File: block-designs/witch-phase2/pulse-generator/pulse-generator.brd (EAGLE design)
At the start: 159.8 x 99.1 mm, 63 parts, among them IC1 74LVC1G08DBV, IC10 74LVC1G08DBV, IC11 741G175, IC12 74LVC1G08DBV, IC13 741G175, IC14 741G175, IC15 741G175, IC16 74LVC1G04DBV, IC17 741G175, IC18 74LVC1G04DBV, IC19 74LVC1G04DBV, IC2 741G175, IC20 NE555D, IC21 74LVC1G17DBV, IC22 74LVC1G17DBV, IC23 74LVC1G17DBV, IC3 741G175, IC4 741G175, IC5 74LVC1G04DBV, IC6 74LVC1G08DBV, IC7 741G175, IC8 74LVC1G08DBV, IC9 74LVC1G08DBV, J1 POWER_JACKPTH, Q1 MMBT2907ALT1SMD

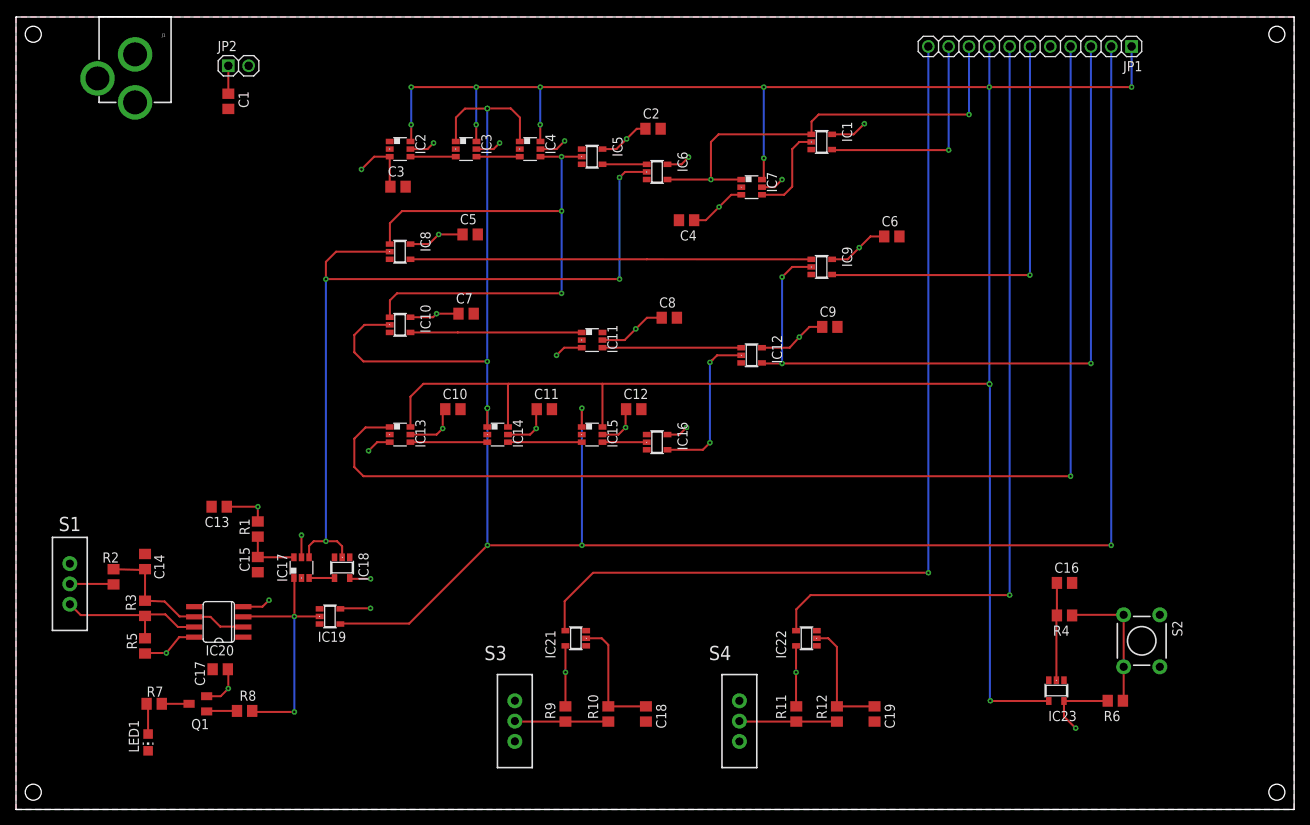
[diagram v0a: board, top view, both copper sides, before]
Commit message: switch position tweaks and drc fixes
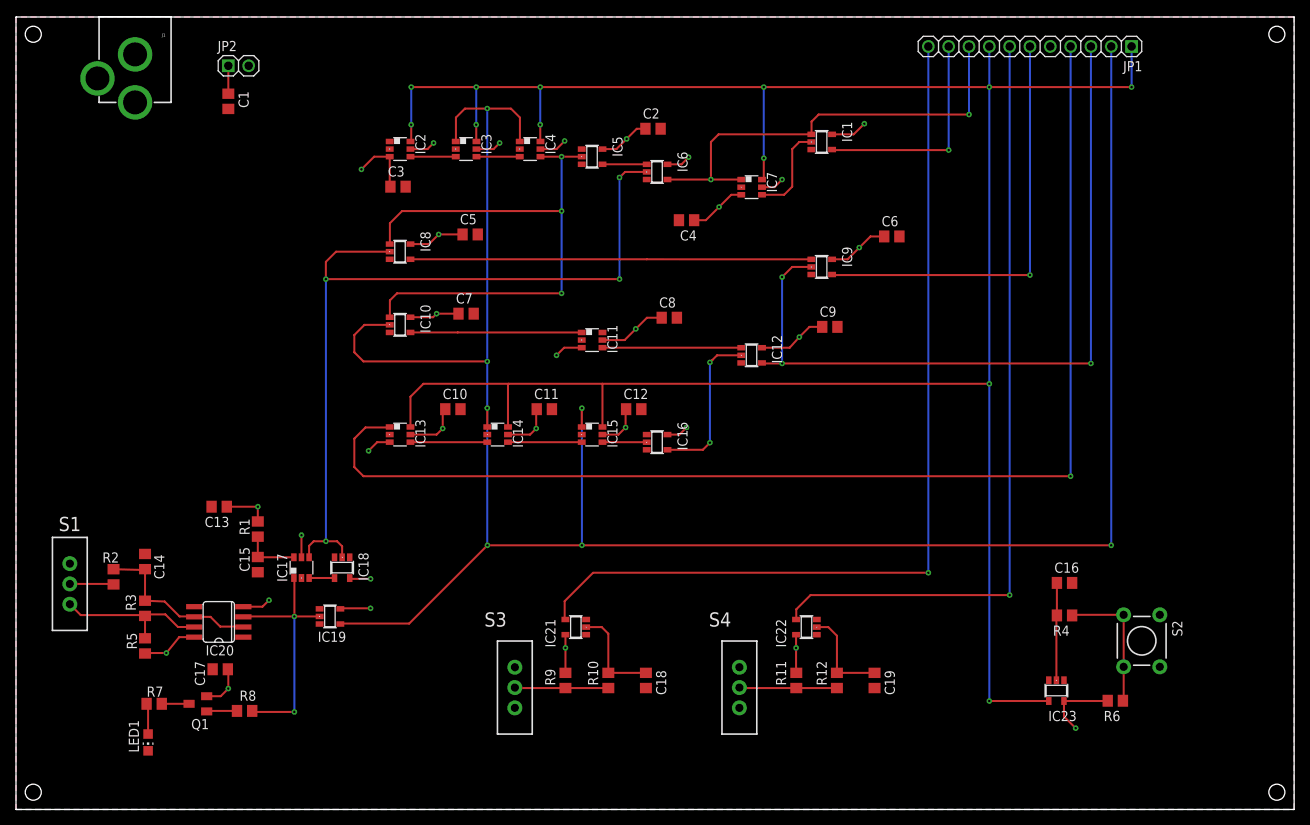
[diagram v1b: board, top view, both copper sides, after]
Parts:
- moved C18 4.19 mm to (78.7, 16.1)
- moved C19 4.19 mm to (107.3, 16.1)
- moved R10 4.19 mm to (74.0, 16.1)
- moved R11 4.19 mm to (97.5, 16.1)
- moved R12 4.19 mm to (102.6, 16.1)
- moved R9 4.19 mm to (68.7, 16.1)
- moved S3 4.19 mm to (62.4, 15.2)
- moved S4 4.19 mm to (90.4, 15.2)
- moved IC21 1.40 mm to (70.0, 22.8)
- moved IC22 1.40 mm to (98.8, 22.8)
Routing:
- net VCC: track 167.7 -> 162.1 mm
- net N$29: track 15.1 -> 12.3 mm
- net N$21: track 15.5 -> 12.7 mm
- net ADD/COMP: track 98.7 -> 97.3 mm
- net CLR: track 116.5 -> 115.1 mm
- net !RST: vias 13 -> 12
- net !MCLK: vias 9 -> 7

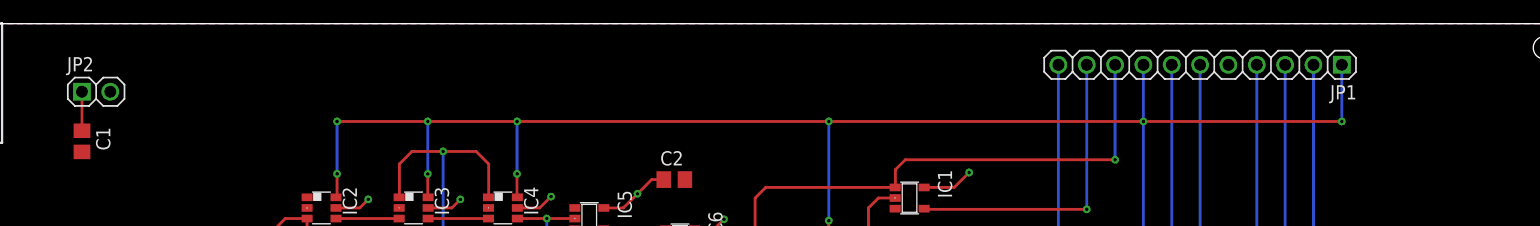
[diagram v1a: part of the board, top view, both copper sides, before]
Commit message: add labels and move downstream power connector
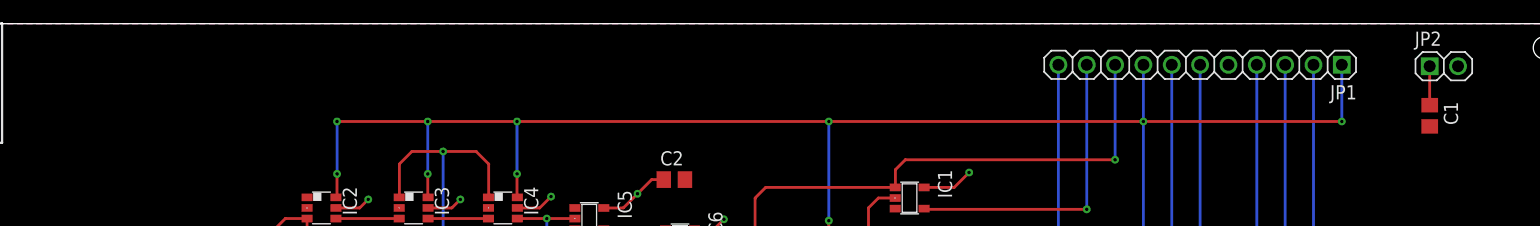
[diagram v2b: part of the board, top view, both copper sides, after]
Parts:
- moved JP2 120.8 mm to (148.6, 95.2)
- moved C1 120.8 mm to (147.3, 90.8)
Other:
- board text added: "ADD/COMP"
- board text added: "CLEAR"
- board text added: "MCLK"
- board text added: "RESET"
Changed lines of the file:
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@@
 <circle x="2.159" y="2.159" radius="2.0066" width="0.0254" layer="42"/>
 <wire x1="159.766" y1="0" x2="0" y2="0" width="0" layer="20"/>
-<text x="36.449" y="91.694" size="2.1844" layer="48">Pulse Generator
+<text x="3.048" y="73.787" size="2.1844" layer="48">Pulse Generator
 http://www.witch-e.org</text>
+<text x="56.388" y="6.096" size="1.778" layer="48">ADD/COMP</text>
+<text x="86.741" y="5.969" size="1.778" layer="48">CLEAR</text>
+<text x="142.113" y="12.446" size="1.778" layer="48">RESET</text>
+<text x="18.923" y="7.239" size="1.778" layer="48">MCLK</text>
 </plain>
 <attributes>
@@
 <element name="IC14" library="witch-e" package="DBV_R-PDSO-G6" value="741G175" x="60.198" y="46.863" rot="R270"/>
 <element name="IC15" library="witch-e" package="DBV_R-PDSO-G6" value="741G175" x="72.009" y="46.863" rot="R270"/>
-<element name="C1" library="resistor" package="C0805" value="10uF" x="26.543" y="88.519" rot="R270"/>
+<element name="C1" library="resistor" package="C0805" value="10uF" x="147.32" y="90.805" rot="R270"/>
 <element name="C17" library="resistor" package="C0805" value="10uF" x="25.527" y="17.526" smashed="yes" rot="R180">
 <attribute name="NAME" x="22.352" y="18.542" size="1.27" layer="25" rot="R270"/>
@@
 <element name="C9" library="resistor" package="C0805" value="1uF" x="101.727" y="60.325"/>
 <element name="C3" library="resistor" package="C0805" value="1uF" x="47.752" y="77.851"/>
-<element name="JP2" library="pinhead" package="1X02" value="" x="27.813" y="92.964"/>
+<element name="JP2" library="pinhead" package="1X02" value="" x="148.59" y="95.25"/>
 <element name="C2" library="resistor" package="C0805" value="10uF" x="79.629" y="85.09"/>
 <element name="C10" library="resistor" package="C0805" value="10uF" x="54.61" y="50.038"/>
@@
 <contactref element="C6" pad="1"/>
 <contactref element="JP2" pad="1"/>
-<wire x1="26.543" y1="89.469" x2="26.543" y2="92.964" width="0.254" layer="1"/>
+<wire x1="147.32" y1="91.755" x2="147.32" y2="95.25" width="0.254" layer="1"/>
 <wire x1="26.477" y1="17.526" x2="26.543" y2="17.46" width="0.254" layer="1"/>
 <wire x1="26.543" y1="17.46" x2="26.543" y2="15.113" width="0.254" layer="1"/>

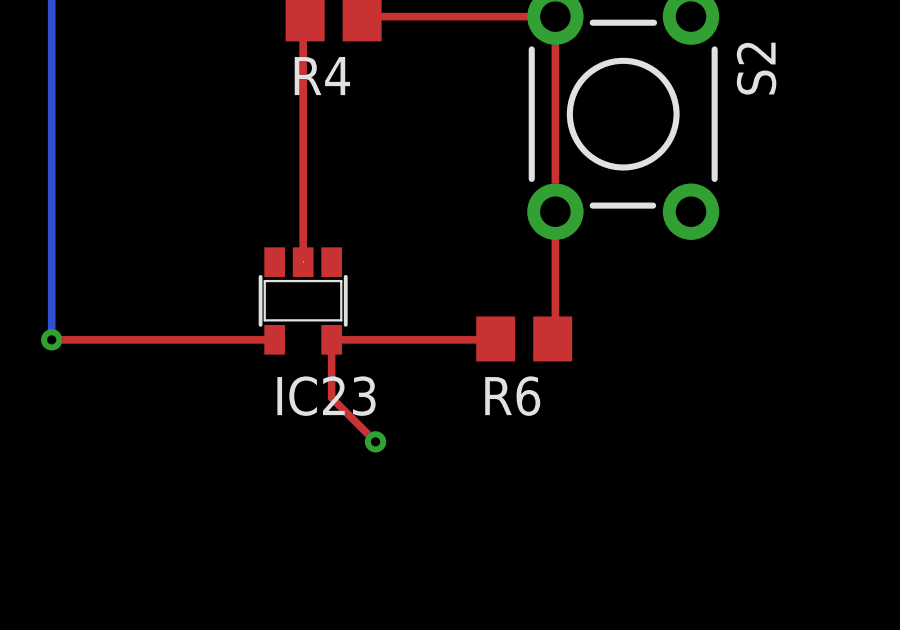
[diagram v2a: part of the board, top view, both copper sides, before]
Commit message: minor changes to position of reset/run button
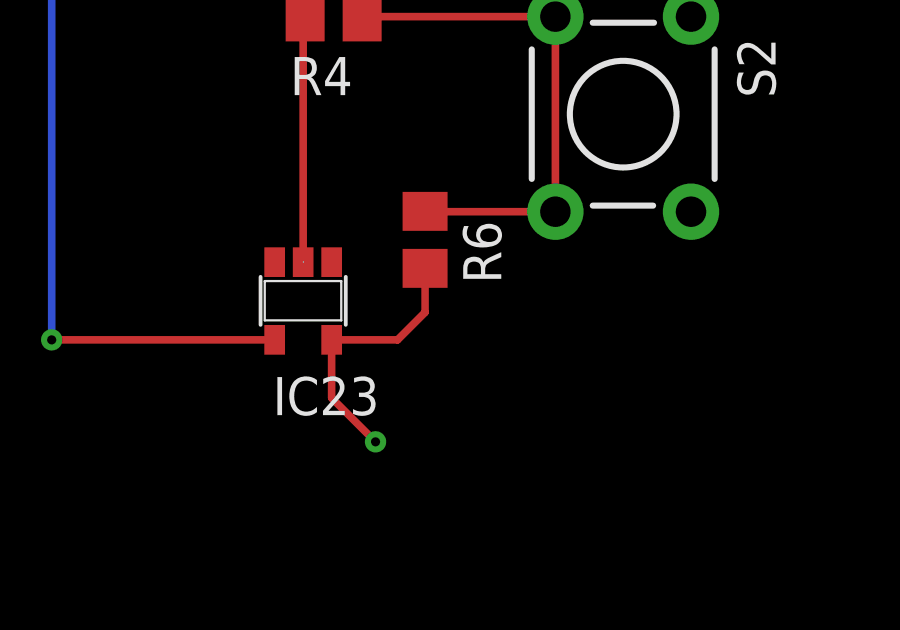
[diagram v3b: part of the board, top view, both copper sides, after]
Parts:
- moved R6 4.67 mm to (134.1, 16.9), turned to 270 degrees
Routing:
- net VCC: track 162.1 -> 161.6 mm
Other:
- board text added: "RESET/RUN"
- board text removed: "RESET"
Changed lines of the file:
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@@
 <text x="56.388" y="6.096" size="1.778" layer="48">ADD/COMP</text>
 <text x="86.741" y="5.969" size="1.778" layer="48">CLEAR</text>
-<text x="142.113" y="12.446" size="1.778" layer="48">RESET</text>
+<text x="134.62" y="10.668" size="1.778" layer="48">RESET/RUN</text>
 <text x="18.923" y="7.239" size="1.778" layer="48">MCLK</text>
 </plain>
@@
 <element name="C16" library="resistor" package="C0805" value="10uF" x="131.064" y="28.321"/>
 <element name="R4" library="resistor" package="R0805" value="10k" x="131.064" y="24.257" rot="R180"/>
-<element name="R6" library="resistor" package="R0805" value="100k" x="137.414" y="13.589" rot="R180"/>
+<element name="R6" library="resistor" package="R0805" value="100k" x="134.112" y="16.891" rot="R270"/>
 <element name="IC23" library="74xx-little-us" package="SOT23-5" value="74LVC1G17DBV" x="130.048" y="14.859" rot="R180"/>
 <element name="JP1" library="pinhead" package="1X11" value="" x="126.746" y="95.377" rot="R180"/>
@@
 <wire x1="100.777" y1="60.325" x2="99.187" y2="60.325" width="0.254" layer="1"/>
 <wire x1="99.187" y1="60.325" x2="97.917" y2="59.055" width="0.254" layer="1"/>
-<wire x1="130.998" y1="13.559" x2="136.434" y2="13.559" width="0.254" layer="1"/>
-<wire x1="136.434" y1="13.559" x2="136.464" y2="13.589" width="0.254" layer="1"/>
 <wire x1="68.677" y1="21.8465" x2="68.6816" y2="21.8419" width="0.254" layer="1"/>
 <via x="68.6816" y="20.193" extent="1-16" drill="0.3048"/>
@@
 <wire x1="49.306" y1="61.529" x2="52.131" y2="61.529" width="0.254" layer="1"/>
 <wire x1="52.131" y1="61.529" x2="52.578" y2="61.976" width="0.254" layer="1"/>
+<wire x1="130.998" y1="13.559" x2="133.193" y2="13.559" width="0.254" layer="1"/>
+<wire x1="133.193" y1="13.559" x2="134.112" y2="14.478" width="0.254" layer="1"/>
+<wire x1="134.112" y1="14.478" x2="134.112" y2="15.941" width="0.254" layer="1"/>
 </signal>
 <signal name="GND">
@@
 <contactref element="S2" pad="4"/>
 <contactref element="R6" pad="1"/>
-<wire x1="138.364" y1="13.589" x2="138.4554" y2="13.6804" width="0.254" layer="1"/>
-<wire x1="138.4554" y1="13.6804" x2="138.4554" y2="17.8308" width="0.254" layer="1"/>
 <wire x1="138.4554" y1="17.8308" x2="138.4554" y2="24.3332" width="0.254" layer="1"/>
 <wire x1="132.014" y1="24.257" x2="132.0902" y2="24.3332" width="0.254" layer="1"/>
 <wire x1="132.0902" y1="24.3332" x2="138.4554" y2="24.3332" width="0.254" layer="1"/>
+<wire x1="138.4554" y1="17.8308" x2="134.1222" y2="17.8308" width="0.254" layer="1"/>
+<wire x1="134.1222" y1="17.8308" x2="134.112" y2="17.841" width="0.254" layer="1"/>
 </signal>
 <signal name="CARRY_DONE">

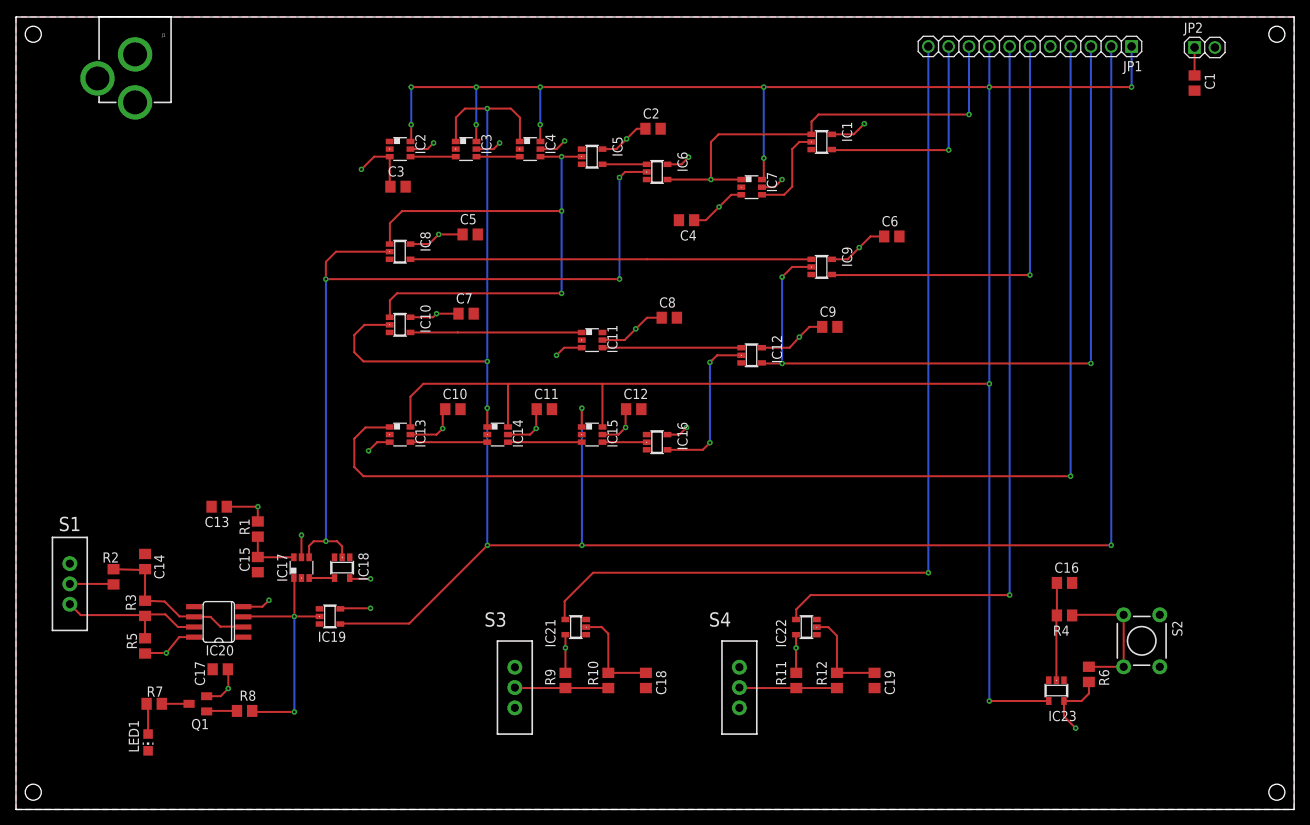
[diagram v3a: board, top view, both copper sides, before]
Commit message: add dekatron sim connector and silkscreen cleanup
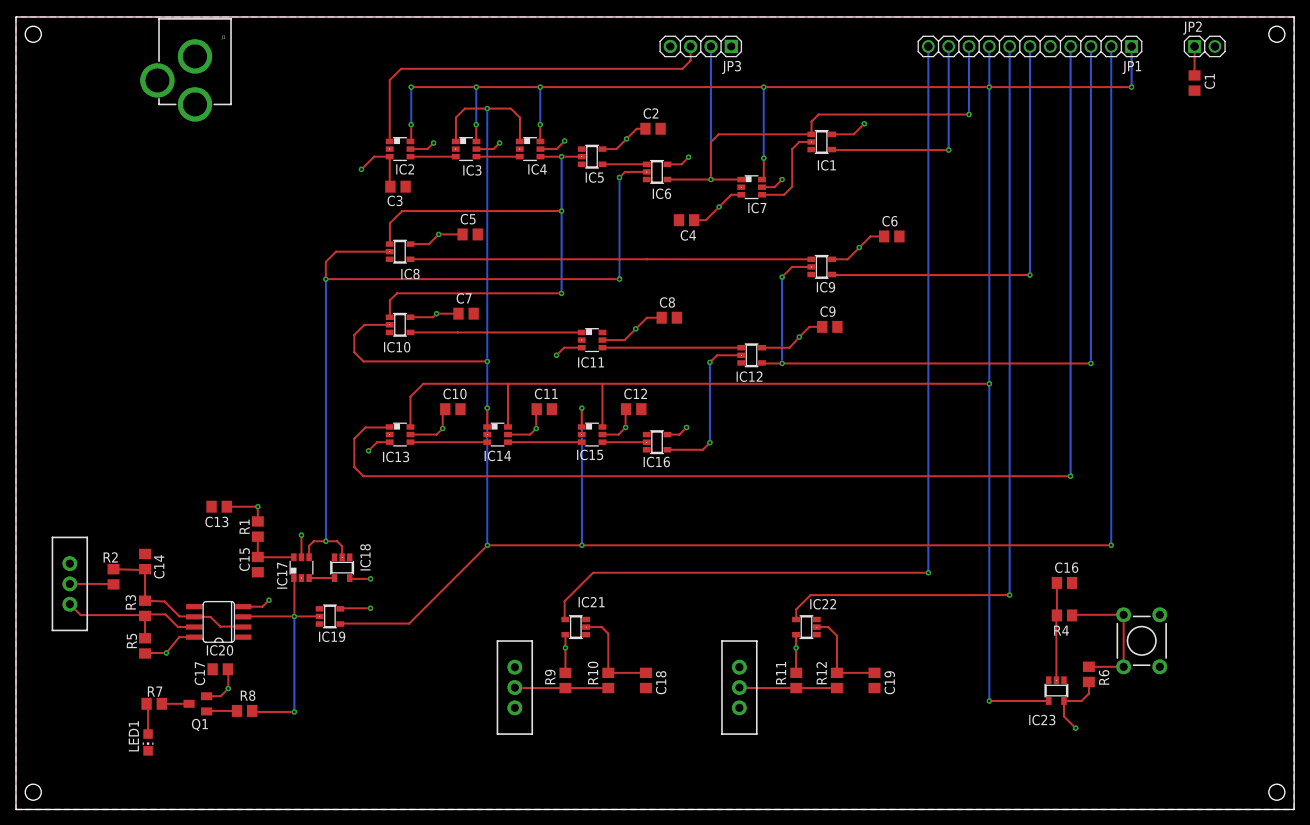
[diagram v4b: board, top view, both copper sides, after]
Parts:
- added JP3: (no value), pinhead:1X04
- moved J1 7.50 mm to (22.4, 101.8)
- moved JP2 0.13 mm to (148.6, 95.4)
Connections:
- net 10A_PULSE: now also JP3.2
- net GND: now also J1.GND, J1.GNDBREAK, JP3.4; no longer J1.PWR
- net VCC: now also J1.PWR, JP3.1; no longer J1.GND, J1.GNDBREAK
- net ZC: now also JP3.3
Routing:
- net ZC: track 0.00 -> 48.1 mm
- net 10A_PULSE: track 57.0 -> 73.7 mm
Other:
- board text added: "Pulse Generator http://witch-e.org"
- board text removed: "Pulse Generator http://www.witch-e.org"

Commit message: remove connection to pin5 on 555
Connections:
- net GND: no longer IC20.5
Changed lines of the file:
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@@
 </signal>
 <signal name="GND">
-<contactref element="IC20" pad="5"/>
 <contactref element="IC20" pad="1"/>
 <contactref element="C14" pad="2"/>
